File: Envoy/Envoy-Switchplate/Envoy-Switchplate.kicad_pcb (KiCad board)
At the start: 2 copper layers, 95.4 x 95.4 mm, 22 parts

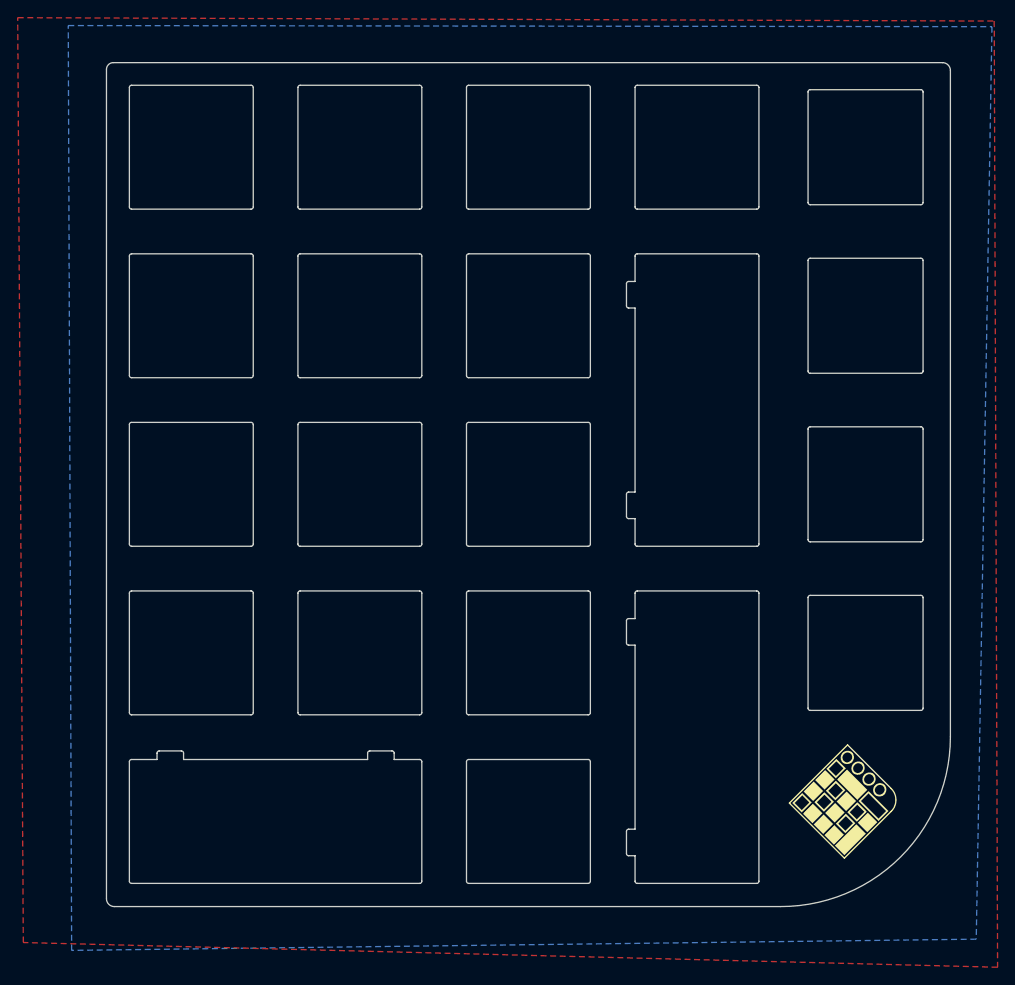
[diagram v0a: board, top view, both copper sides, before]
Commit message: curves!  Fun curved traces.  Prepare rev0.2 gerbers
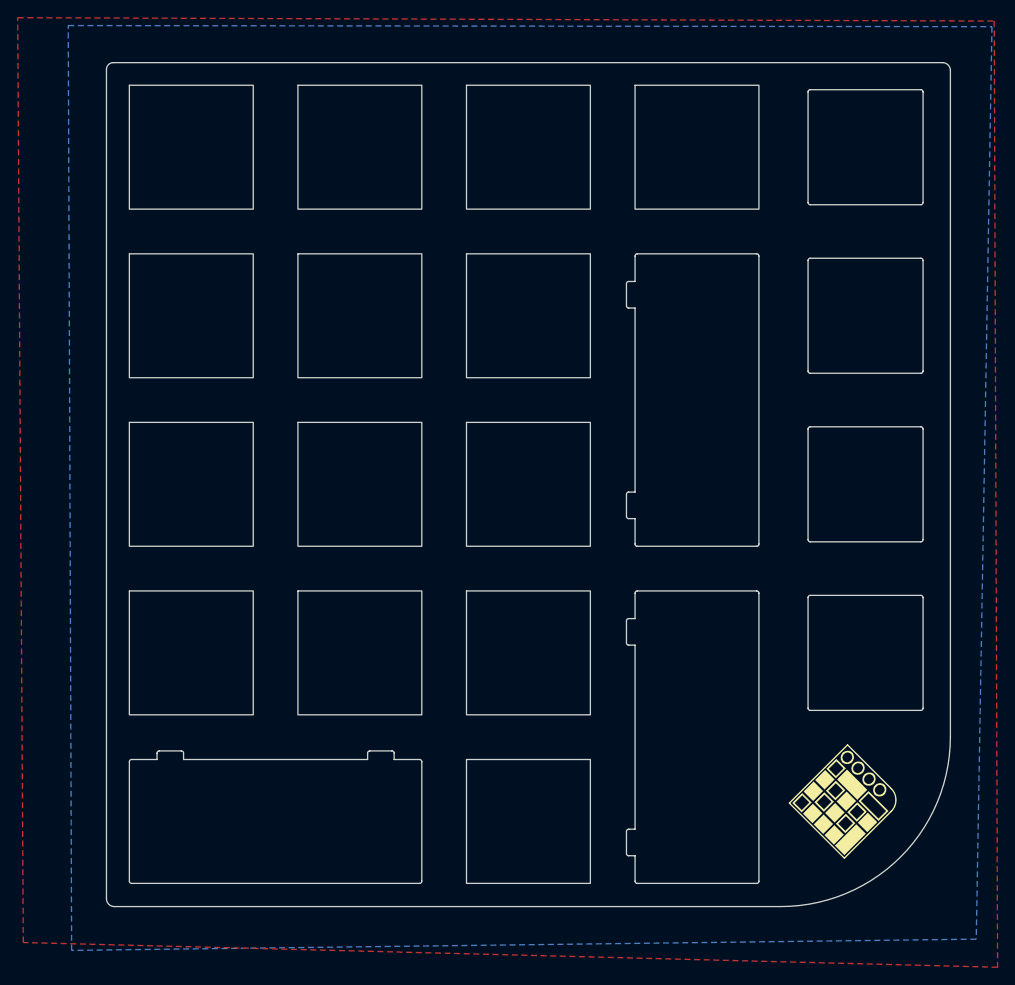
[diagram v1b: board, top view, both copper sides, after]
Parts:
- MX1, MX10, MX11, MX13, MX14, MX15, MX19, MX2, MX3, MX4, MX5, MX6, MX7, MX9: footprint Envoy:MX_Switch_Cutout_Square_fillets -> Envoy:MX_Switch_Cutout_Square

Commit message: Bumped switchplate revision to 1.0.  No design changes from rev 0.2.
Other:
- board text added: "Envoy by JeJeff - switch plate - rev 1.0"
- board text removed: "Envoy by JeJeff - switch plate - rev 0.2"
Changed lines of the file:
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@@
     (effects (font (size 0.85 0.85) (thickness 0.15)) (justify mirror))
   )
-  (gr_text "Envoy by JeJeff - switch plate - rev 0.2" (at 140.6655 123.45075) (layer "B.Mask")
+  (gr_text "Envoy by JeJeff - switch plate - rev 1.0" (at 140.6655 123.45075) (layer "B.Mask")
     (effects (font (size 1 1) (thickness 0.15)) (justify mirror))
   )
